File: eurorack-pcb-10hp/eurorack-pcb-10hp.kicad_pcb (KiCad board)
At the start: 2 copper layers, 59.1 x 108.3 mm, 0 parts

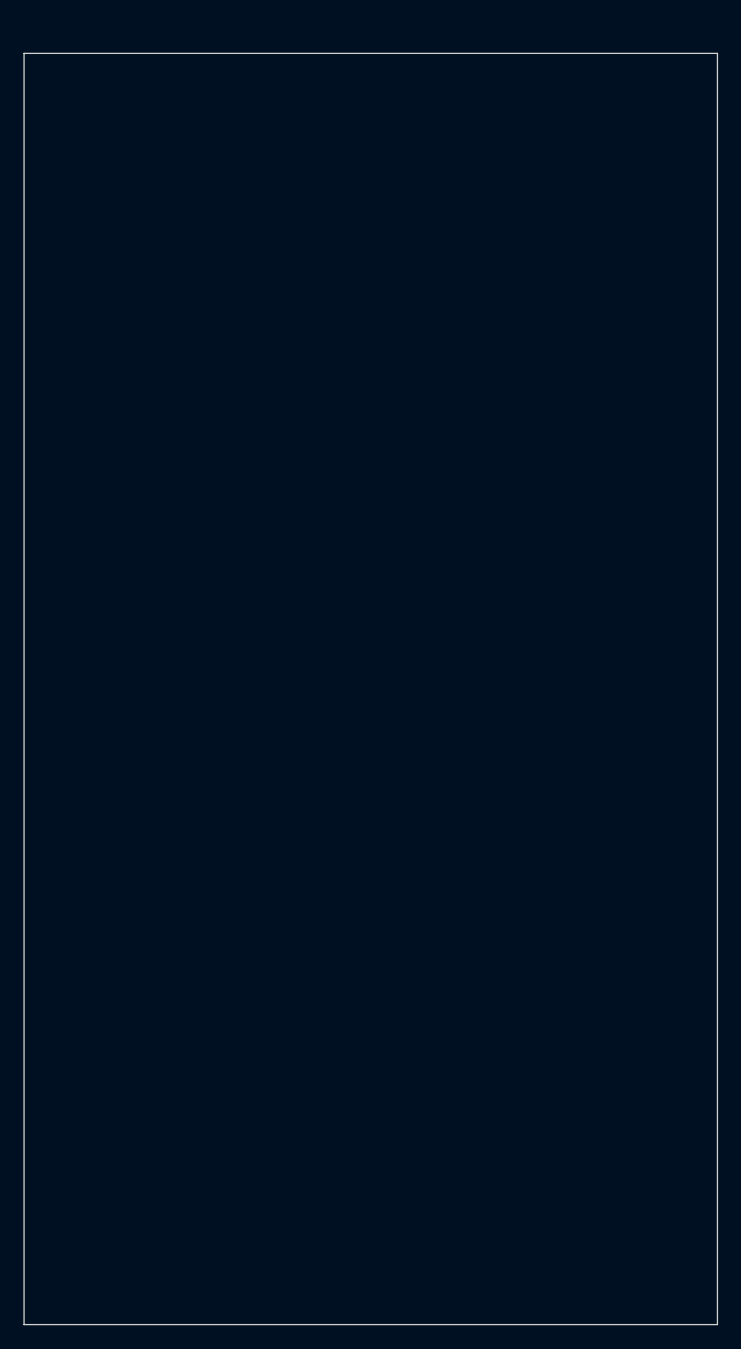
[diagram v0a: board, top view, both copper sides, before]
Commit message: Minor adjustments to PCB positioning. Moving everything into a single folder to be easier for kiCad to pick up all templates from user-template path
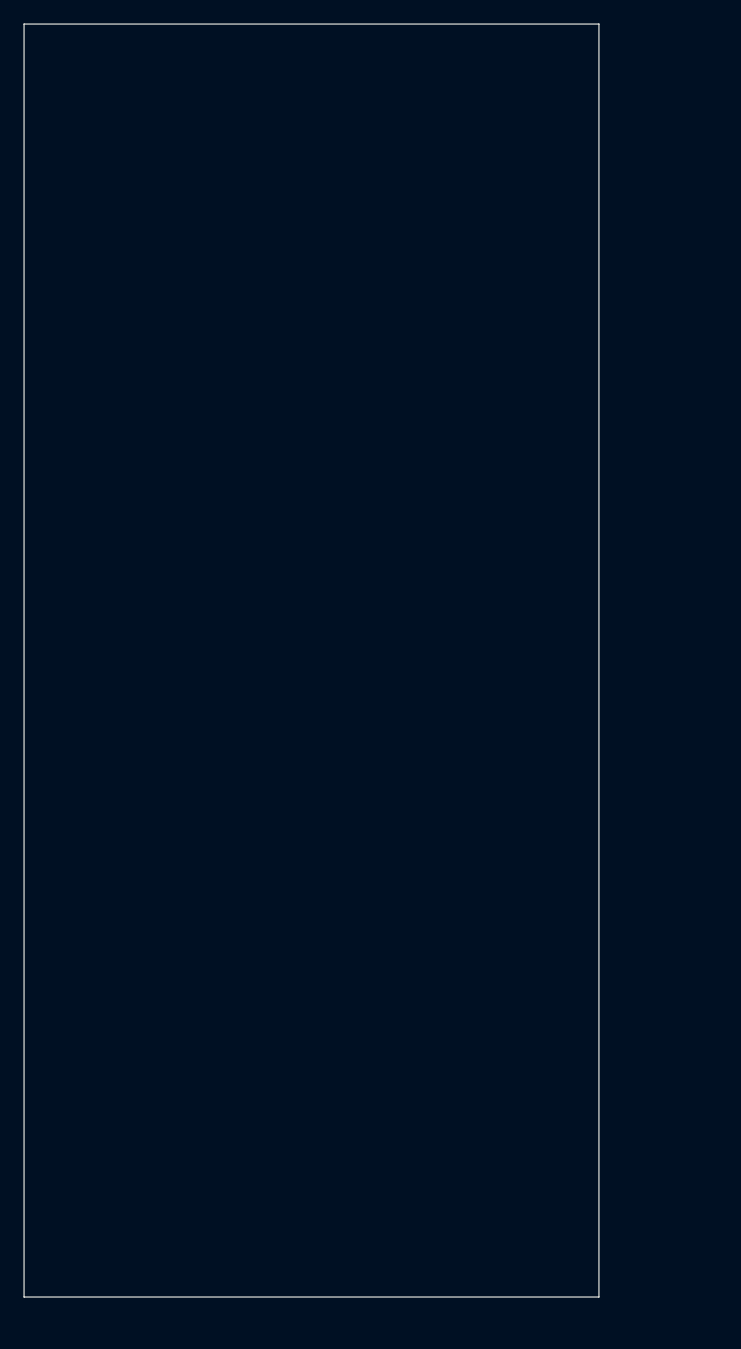
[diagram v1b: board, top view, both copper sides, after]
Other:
- board size 59.1 x 108.3 mm -> 49 x 108.5 mm
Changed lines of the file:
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@@
   )
   (net 0 "")
-  (gr_line (start 0.75 12.5) (end 0.75 120.85) (layer "Edge.Cuts") (width 0.1))
-  (gr_line (start 59.85 120.85) (end 59.85 12.5) (layer "Edge.Cuts") (width 0.1))
-  (gr_line (start 0.75 120.85) (end 59.85 120.85) (layer "Edge.Cuts") (width 0.1))
-  (gr_line (start 0.75 12.5) (end 59.85 12.5) (layer "Edge.Cuts") (width 0.1))
-  (gr_line (start 60.6 0) (end 60.6 128.5) (layer "User.1") (width 0.1))
+  (gr_line (start 0.75 10) (end 0.75 118.5) (layer "Edge.Cuts") (width 0.1))
+  (gr_line (start 49.75 118.5) (end 49.75 10) (layer "Edge.Cuts") (width 0.1))
+  (gr_line (start 0.75 118.5) (end 49.75 118.5) (layer "Edge.Cuts") (width 0.1))
+  (gr_line (start 0.75 10) (end 49.75 10) (layer "Edge.Cuts") (width 0.1))
+  (gr_line (start 50.5 0) (end 50.5 128.5) (layer "User.1") (width 0.1))
   (gr_line (start 0 128.5) (end 0 0) (layer "User.1") (width 0.1))
-  (gr_line (start 0 0) (end 60.6 0) (layer "User.1") (width 0.1))
-  (gr_line (start 60.6 128.5) (end 0 128.5) (layer "User.1") (width 0.1))
+  (gr_line (start 0 0) (end 50.5 0) (layer "User.1") (width 0.1))
+  (gr_line (start 50.5 128.5) (end 0 128.5) (layer "User.1") (width 0.1))
 )
